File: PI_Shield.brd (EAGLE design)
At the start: 78.7 x 69.5 mm, 64 parts, among them Q1 220mA/50V/3.5Ω, Q3 220mA/50V/3.5Ω, Q4 220mA/50V/3.5Ω, Q5 2.5A/30V/105mΩ, U1 MAX1136EUA-T, U2 AZ1117EH-3.3TRG1, Y1 ECS-80-S-4X

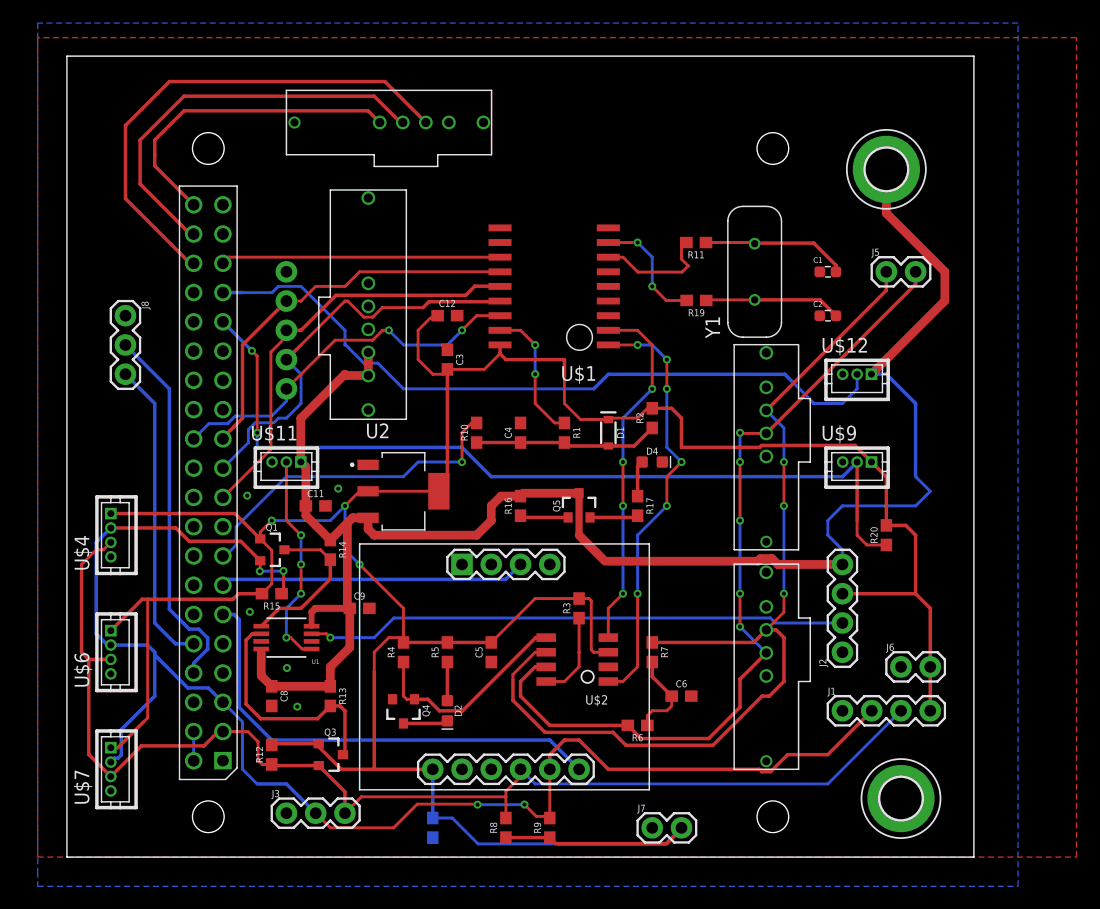
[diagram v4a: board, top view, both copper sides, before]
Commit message: Outline change
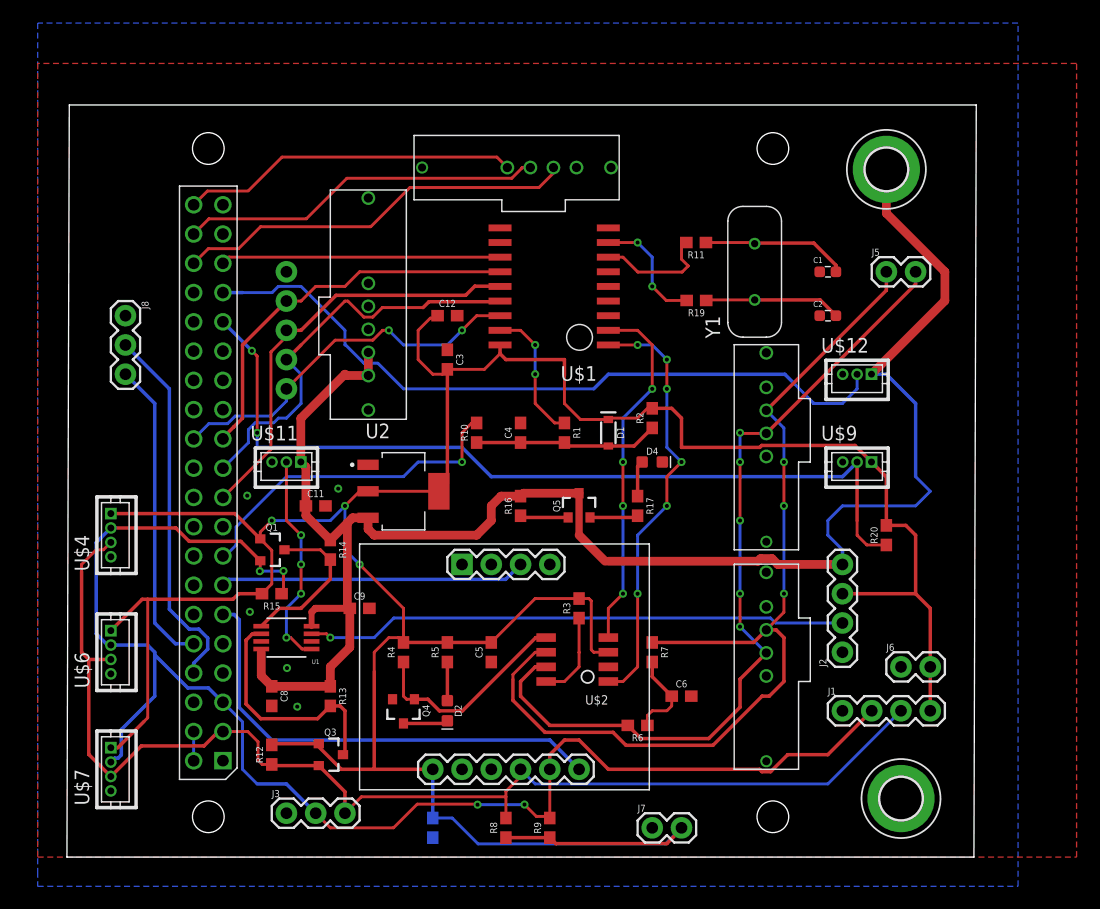
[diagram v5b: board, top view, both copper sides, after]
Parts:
- moved U$14 11.7 mm to (44.1, 65.9)
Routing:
- net DI1: track 43.7 -> 34.9 mm
- net DI2: track 35.6 -> 31.6 mm
- net DI3: track 28.0 -> 29.3 mm
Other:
- board size 78.7 x 69.5 mm -> 78.9 x 65.3 mm
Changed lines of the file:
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@@
 <plain>
 <wire x1="13.97" y1="8.89" x2="92.69" y2="8.89" width="0" layer="20"/>
-<wire x1="92.69" y1="8.89" x2="92.69" y2="78.41" width="0" layer="20"/>
-<wire x1="92.69" y1="78.41" x2="13.97" y2="78.41" width="0" layer="20"/>
-<wire x1="13.97" y1="78.41" x2="13.97" y2="8.89" width="0" layer="20"/>
+<wire x1="92.69" y1="8.89" x2="92.8932" y2="74.1682" width="0" layer="20"/>
+<wire x1="92.8932" y1="74.1682" x2="14.1732" y2="74.1682" width="0" layer="20"/>
+<wire x1="14.1732" y1="74.1682" x2="13.97" y2="8.89" width="0" layer="20"/>
 </plain>
 <attributes>
@@
 </element>
 <element name="U$13" library="BackplaneParts" package="T2I" value="T2I" x="77.47" y="35.56" smashed="yes" rot="R90"/>
-<element name="U$14" library="BackplaneParts" package="T2I" value="T2I" x="33.02" y="69.85" smashed="yes"/>
+<element name="U$14" library="BackplaneParts" package="T2I" value="T2I" x="44.0944" y="65.9384" smashed="yes"/>
 <element name="U$2" library="PI_Shield_Library" package="TCAN337D" value="TCAN337D" x="60.96" y="27.94" smashed="yes" rot="R180">
 <attribute name="NAME" x="60.96" y="22.94" size="0.8128" layer="25" rot="R180"/>
@@
 <contactref element="PCB1" pad="P$39"/>
 <polygon width="0.1524" layer="1">
-<vertex x="11.43" y="80.01"/>
+<vertex x="11.43" y="77.7748"/>
 <vertex x="11.43" y="8.89"/>
 <vertex x="101.6" y="8.89"/>
-<vertex x="101.6" y="80.01"/>
+<vertex x="101.6" y="77.7748"/>
 </polygon>
 <polygon width="0.254" layer="16">
@@
 <contactref element="U$14" pad="3"/>
 <contactref element="PCB1" pad="P$36"/>
-<wire x1="45.12" y1="72.65" x2="41.57" y2="76.2" width="0.3048" layer="1"/>
-<wire x1="22.86" y1="76.2" x2="19.05" y2="72.39" width="0.3048" layer="1"/>
-<wire x1="19.05" y1="72.39" x2="19.05" y2="66.04" width="0.3048" layer="1"/>
-<wire x1="19.05" y1="66.04" x2="24.6634" y2="60.4266" width="0.3048" layer="1"/>
-<wire x1="24.6634" y1="60.4266" x2="24.9682" y2="60.4266" width="0.3048" layer="1"/>
-<wire x1="41.57" y1="76.2" x2="22.86" y2="76.2" width="0.3048" layer="1"/>
+<wire x1="56.1944" y1="68.7384" x2="56.1944" y2="68.2594" width="0.254" layer="1"/>
+<wire x1="56.1944" y1="68.2594" x2="54.9402" y2="67.0052" width="0.254" layer="1"/>
+<wire x1="54.9402" y1="67.0052" x2="43.7388" y2="67.0052" width="0.254" layer="1"/>
+<wire x1="43.7388" y1="67.0052" x2="40.3352" y2="63.6016" width="0.254" layer="1"/>
+<wire x1="40.3352" y1="63.6016" x2="30.7694875" y2="63.6016" width="0.254" layer="1"/>
+<wire x1="30.7694875" y1="63.6016" x2="28.8644875" y2="61.6966" width="0.254" layer="1"/>
+<wire x1="28.8644875" y1="61.6966" x2="26.2382" y2="61.6966" width="0.254" layer="1"/>
+<wire x1="26.2382" y1="61.6966" x2="24.9682" y2="60.4266" width="0.254" layer="1"/>
 </signal>
 <signal name="DI2">
 <contactref element="U$14" pad="2"/>
 <contactref element="PCB1" pad="P$38"/>
-<wire x1="43.12" y1="72.65" x2="42.92" y2="72.65" width="0.3048" layer="1"/>
-<wire x1="42.92" y1="72.65" x2="40.64" y2="74.93" width="0.3048" layer="1"/>
-<wire x1="40.64" y1="74.93" x2="24.13" y2="74.93" width="0.3048" layer="1"/>
-<wire x1="20.32" y1="71.12" x2="20.32" y2="67.31" width="0.3048" layer="1"/>
-<wire x1="20.32" y1="67.31" x2="24.6634" y2="62.9666" width="0.3048" layer="1"/>
-<wire x1="24.6634" y1="62.9666" x2="24.9682" y2="62.9666" width="0.3048" layer="1"/>
-<wire x1="24.13" y1="74.93" x2="20.32" y2="71.12" width="0.3048" layer="1"/>
+<wire x1="53.47398125" y1="68.7384" x2="54.1944" y2="68.7384" width="0.254" layer="1"/>
+<wire x1="24.9682" y1="62.9666" x2="26.289" y2="64.2874" width="0.254" layer="1"/>
+<wire x1="52.57970625" y1="67.8082" x2="53.47398125" y2="68.702475" width="0.254" layer="1"/>
+<wire x1="53.47398125" y1="68.702475" x2="53.47398125" y2="68.7384" width="0.254" layer="1"/>
+<wire x1="34.7472" y1="64.2874" x2="38.268" y2="67.8082" width="0.254" layer="1"/>
+<wire x1="38.268" y1="67.8082" x2="52.57970625" y2="67.8082" width="0.254" layer="1"/>
+<wire x1="26.289" y1="64.2874" x2="34.7472" y2="64.2874" width="0.254" layer="1"/>
 </signal>
 <signal name="DI3">
 <contactref element="U$14" pad="1"/>
 <contactref element="PCB1" pad="P$40"/>
-<wire x1="41.12" y1="72.65" x2="40.11" y2="73.66" width="0.3048" layer="1"/>
-<wire x1="24.13" y1="73.66" x2="21.59" y2="71.12" width="0.3048" layer="1"/>
-<wire x1="21.59" y1="71.12" x2="21.59" y2="69.85" width="0.3048" layer="1"/>
-<wire x1="21.59" y1="69.85" x2="21.59" y2="68.8848" width="0.3048" layer="1"/>
-<wire x1="21.59" y1="68.8848" x2="24.9682" y2="65.5066" width="0.3048" layer="1"/>
-<wire x1="40.11" y1="73.66" x2="24.13" y2="73.66" width="0.3048" layer="1"/>
+<wire x1="32.6394" y1="69.6472" x2="51.2856" y2="69.6472" width="0.254" layer="1"/>
+<wire x1="29.6926" y1="66.7004" x2="29.7688" y2="66.7766" width="0.2032" layer="1"/>
+<wire x1="24.9682" y1="65.5066" x2="26.162" y2="66.7004" width="0.254" layer="1"/>
+<wire x1="26.162" y1="66.7004" x2="29.6926" y2="66.7004" width="0.254" layer="1"/>
+<wire x1="29.7688" y1="66.7766" x2="32.6394" y2="69.6472" width="0.254" layer="1"/>
+<wire x1="51.2856" y1="69.6472" x2="52.1944" y2="68.7384" width="0.254" layer="1"/>
 </signal>
 <signal name="N$7">

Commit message: Update PI_Shield.brd
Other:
- board size 78.9 x 65.3 mm -> 78.8 x 65.3 mm
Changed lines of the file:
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@@
 <plain>
 <wire x1="13.97" y1="8.89" x2="92.69" y2="8.89" width="0" layer="20"/>
-<wire x1="92.69" y1="8.89" x2="92.8932" y2="74.1682" width="0" layer="20"/>
-<wire x1="92.8932" y1="74.1682" x2="14.1732" y2="74.1682" width="0" layer="20"/>
-<wire x1="14.1732" y1="74.1682" x2="13.97" y2="8.89" width="0" layer="20"/>
+<wire x1="92.69" y1="8.89" x2="92.7408" y2="74.1682" width="0" layer="20"/>
+<wire x1="92.7408" y1="74.1682" x2="14.0208" y2="74.1682" width="0" layer="20"/>
+<wire x1="14.0208" y1="74.1682" x2="13.97" y2="8.89" width="0" layer="20"/>
 </plain>
 <attributes>

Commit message: Update PI_Shield.brd
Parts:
- moved J8 7.75 mm to (19.3, 48.1)
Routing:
- net TX: track 32.4 -> 24.6 mm
- net RX: track 26.8 -> 18.9 mm
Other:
- board size 78.8 x 65.3 mm -> 77.6 x 65.3 mm
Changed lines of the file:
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@@
 <board>
 <plain>
-<wire x1="13.97" y1="8.89" x2="92.69" y2="8.89" width="0" layer="20"/>
-<wire x1="92.69" y1="8.89" x2="92.7408" y2="74.1682" width="0" layer="20"/>
-<wire x1="92.7408" y1="74.1682" x2="14.0208" y2="74.1682" width="0" layer="20"/>
+<wire x1="13.97" y1="8.89" x2="91.5216" y2="8.89" width="0" layer="20"/>
+<wire x1="91.5216" y1="8.89" x2="91.5724" y2="74.1682" width="0" layer="20"/>
+<wire x1="91.5724" y1="74.1682" x2="14.0208" y2="74.1682" width="0" layer="20"/>
 <wire x1="14.0208" y1="74.1682" x2="13.97" y2="8.89" width="0" layer="20"/>
 </plain>
@@
 <attribute name="VALUE" x="63.5" y="9.398" size="0.6096" layer="27" font="vector" ratio="20"/>
 </element>
-<element name="J8" library="SparkFun-Connectors" library_urn="urn:adsk.eagle:library:513" package="1X03" package3d_urn="urn:adsk.eagle:package:38063/1" value="" x="19.05" y="55.88" smashed="yes" rot="R270">
-<attribute name="NAME" x="20.447" y="57.15" size="0.6096" layer="25" font="vector" ratio="20" rot="R270"/>
-<attribute name="VALUE" x="17.018" y="57.15" size="0.6096" layer="27" font="vector" ratio="20" rot="R270"/>
+<element name="J8" library="SparkFun-Connectors" library_urn="urn:adsk.eagle:library:513" package="1X03" package3d_urn="urn:adsk.eagle:package:38063/1" value="" x="19.2532" y="48.133" smashed="yes" rot="R270">
+<attribute name="NAME" x="20.6502" y="49.403" size="0.6096" layer="25" font="vector" ratio="20" rot="R270"/>
+<attribute name="VALUE" x="17.2212" y="49.403" size="0.6096" layer="27" font="vector" ratio="20" rot="R270"/>
 </element>
 <element name="PCB1" library="MicrocontrollerComponents" package="RPI2" value="RPI2" x="78.74" y="8.89" smashed="yes" rot="R90"/>
@@
 <contactref element="PCB1" pad="P$36"/>
 <wire x1="56.1944" y1="68.7384" x2="56.1944" y2="68.2594" width="0.254" layer="1"/>
-<wire x1="56.1944" y1="68.2594" x2="54.9402" y2="67.0052" width="0.254" layer="1"/>
-<wire x1="54.9402" y1="67.0052" x2="43.7388" y2="67.0052" width="0.254" layer="1"/>
-<wire x1="43.7388" y1="67.0052" x2="40.3352" y2="63.6016" width="0.254" layer="1"/>
-<wire x1="40.3352" y1="63.6016" x2="30.7694875" y2="63.6016" width="0.254" layer="1"/>
-<wire x1="30.7694875" y1="63.6016" x2="28.8644875" y2="61.6966" width="0.254" layer="1"/>
+<wire x1="56.1944" y1="68.2594" x2="54.991" y2="67.056" width="0.254" layer="1"/>
+<wire x1="54.991" y1="67.056" x2="34.2238875" y2="67.056" width="0.254" layer="1"/>
+<wire x1="34.2238875" y1="67.056" x2="28.8644875" y2="61.6966" width="0.254" layer="1"/>
 <wire x1="28.8644875" y1="61.6966" x2="26.2382" y2="61.6966" width="0.254" layer="1"/>
 <wire x1="26.2382" y1="61.6966" x2="24.9682" y2="60.4266" width="0.254" layer="1"/>
@@
 <wire x1="52.57970625" y1="67.8082" x2="53.47398125" y2="68.702475" width="0.254" layer="1"/>
 <wire x1="53.47398125" y1="68.702475" x2="53.47398125" y2="68.7384" width="0.254" layer="1"/>
-<wire x1="34.7472" y1="64.2874" x2="38.268" y2="67.8082" width="0.254" layer="1"/>
-<wire x1="38.268" y1="67.8082" x2="52.57970625" y2="67.8082" width="0.254" layer="1"/>
-<wire x1="26.289" y1="64.2874" x2="34.7472" y2="64.2874" width="0.254" layer="1"/>
+<wire x1="29.21" y1="64.2874" x2="32.7308" y2="67.8082" width="0.254" layer="1"/>
+<wire x1="32.7308" y1="67.8082" x2="52.57970625" y2="67.8082" width="0.254" layer="1"/>
+<wire x1="26.289" y1="64.2874" x2="29.21" y2="64.2874" width="0.254" layer="1"/>
 </signal>
 <signal name="DI3">
@@
 <contactref element="J8" pad="2"/>
 <contactref element="PCB1" pad="P$8"/>
-<wire x1="19.05" y1="53.34" x2="22.86" y2="49.53" width="0.3048" layer="16"/>
+<wire x1="19.2532" y1="45.593" x2="22.86" y2="41.9862" width="0.3048" layer="16"/>
 <wire x1="24.5872" y1="28.6766" x2="25.4100875" y2="28.6766" width="0.3048" layer="16"/>
 <wire x1="25.4100875" y1="28.6766" x2="26.1874" y2="27.8992875" width="0.3048" layer="16"/>
@@
 <wire x1="24.9682" y1="25.7201125" x2="24.9682" y2="24.8666" width="0.3048" layer="16"/>
 <wire x1="26.1874" y1="26.9393125" x2="24.9682" y2="25.7201125" width="0.3048" layer="16"/>
-<wire x1="22.86" y1="49.53" x2="22.86" y2="30.4038" width="0.3048" layer="16"/>
+<wire x1="22.86" y1="41.9862" x2="22.86" y2="30.4038" width="0.3048" layer="16"/>
 <wire x1="22.86" y1="30.4038" x2="24.5872" y2="28.6766" width="0.3048" layer="16"/>
 </signal>
@@
 <contactref element="J8" pad="3"/>
 <contactref element="PCB1" pad="P$10"/>
-<wire x1="19.05" y1="50.8" x2="21.59" y2="48.26" width="0.3048" layer="16"/>
-<wire x1="21.59" y1="48.26" x2="21.59" y2="29.21" width="0.3048" layer="16"/>
+<wire x1="19.2532" y1="43.053" x2="21.59" y2="40.7162" width="0.3048" layer="16"/>
+<wire x1="21.59" y1="40.7162" x2="21.59" y2="29.21" width="0.3048" layer="16"/>
 <wire x1="21.59" y1="29.21" x2="23.3934" y2="27.4066" width="0.3048" layer="16"/>
 <wire x1="23.3934" y1="27.4066" x2="24.9682" y2="27.4066" width="0.3048" layer="16"/>

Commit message: Update PI_Shield.brd
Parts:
- moved J8 1.85 mm to (20.9, 47.3)
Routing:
- net RX: track 18.9 -> 17.4 mm
- net TX: track 24.6 -> 23.1 mm
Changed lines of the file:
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@@
 <attribute name="VALUE" x="63.5" y="9.398" size="0.6096" layer="27" font="vector" ratio="20"/>
 </element>
-<element name="J8" library="SparkFun-Connectors" library_urn="urn:adsk.eagle:library:513" package="1X03" package3d_urn="urn:adsk.eagle:package:38063/1" value="" x="19.2532" y="48.133" smashed="yes" rot="R270">
-<attribute name="NAME" x="20.6502" y="49.403" size="0.6096" layer="25" font="vector" ratio="20" rot="R270"/>
-<attribute name="VALUE" x="17.2212" y="49.403" size="0.6096" layer="27" font="vector" ratio="20" rot="R270"/>
+<element name="J8" library="SparkFun-Connectors" library_urn="urn:adsk.eagle:library:513" package="1X03" package3d_urn="urn:adsk.eagle:package:38063/1" value="" x="20.9042" y="47.2948" smashed="yes" rot="R270">
+<attribute name="NAME" x="22.3012" y="48.5648" size="0.6096" layer="25" font="vector" ratio="20" rot="R270"/>
+<attribute name="VALUE" x="18.8722" y="48.5648" size="0.6096" layer="27" font="vector" ratio="20" rot="R270"/>
 </element>
 <element name="PCB1" library="MicrocontrollerComponents" package="RPI2" value="RPI2" x="78.74" y="8.89" smashed="yes" rot="R90"/>
@@
 </polygon>
 <polygon width="0.254" layer="16">
-<vertex x="11.43" y="81.28"/>
-<vertex x="11.43" y="7.62"/>
-<vertex x="11.43" y="6.35"/>
+<vertex x="10.16" y="81.28"/>
+<vertex x="10.16" y="6.35"/>
 <vertex x="96.52" y="6.35"/>
 <vertex x="96.52" y="81.28"/>
-<vertex x="92.71" y="81.28"/>
 </polygon>
 <via x="29.6164" y="40.259" extent="1-16" drill="0.35"/>
@@
 <contactref element="J8" pad="2"/>
 <contactref element="PCB1" pad="P$8"/>
-<wire x1="19.2532" y1="45.593" x2="22.86" y2="41.9862" width="0.3048" layer="16"/>
+<wire x1="20.9042" y1="44.7548" x2="22.86" y2="42.799" width="0.3048" layer="16"/>
 <wire x1="24.5872" y1="28.6766" x2="25.4100875" y2="28.6766" width="0.3048" layer="16"/>
 <wire x1="25.4100875" y1="28.6766" x2="26.1874" y2="27.8992875" width="0.3048" layer="16"/>
@@
 <wire x1="24.9682" y1="25.7201125" x2="24.9682" y2="24.8666" width="0.3048" layer="16"/>
 <wire x1="26.1874" y1="26.9393125" x2="24.9682" y2="25.7201125" width="0.3048" layer="16"/>
-<wire x1="22.86" y1="41.9862" x2="22.86" y2="30.4038" width="0.3048" layer="16"/>
+<wire x1="22.86" y1="42.799" x2="22.86" y2="30.4038" width="0.3048" layer="16"/>
 <wire x1="22.86" y1="30.4038" x2="24.5872" y2="28.6766" width="0.3048" layer="16"/>
 </signal>
@@
 <contactref element="J8" pad="3"/>
 <contactref element="PCB1" pad="P$10"/>
-<wire x1="19.2532" y1="43.053" x2="21.59" y2="40.7162" width="0.3048" layer="16"/>
-<wire x1="21.59" y1="40.7162" x2="21.59" y2="29.21" width="0.3048" layer="16"/>
+<wire x1="20.9042" y1="42.2148" x2="21.59" y2="41.529" width="0.3048" layer="16"/>
+<wire x1="21.59" y1="41.529" x2="21.59" y2="29.21" width="0.3048" layer="16"/>
 <wire x1="21.59" y1="29.21" x2="23.3934" y2="27.4066" width="0.3048" layer="16"/>
 <wire x1="23.3934" y1="27.4066" x2="24.9682" y2="27.4066" width="0.3048" layer="16"/>
